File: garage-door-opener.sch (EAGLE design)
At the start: 17 parts, among them IC1 LM2575-3.3T, K1 RR1A, T1 BC547, U1 ESP8266, X2 Connector

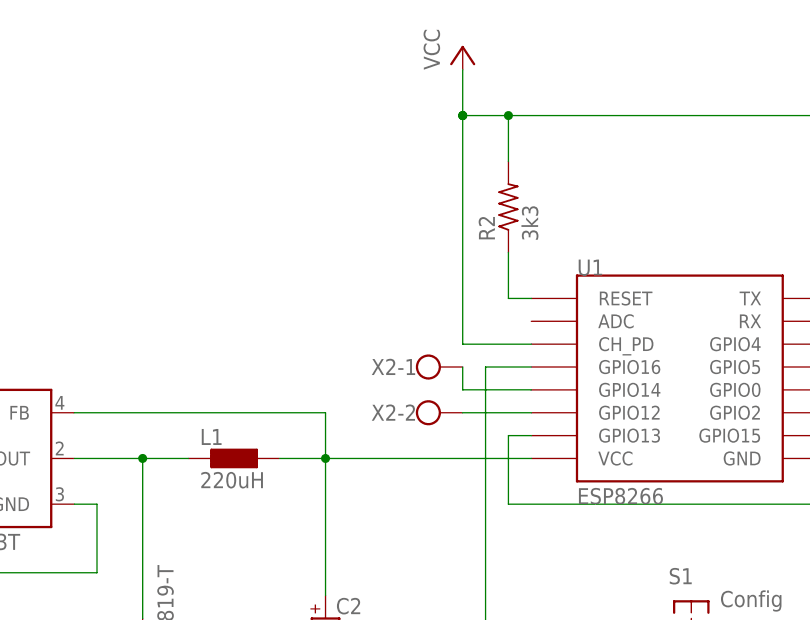
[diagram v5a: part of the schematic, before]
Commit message: removed all the vias. Re-routed some tracks around the developer holes (sort of)
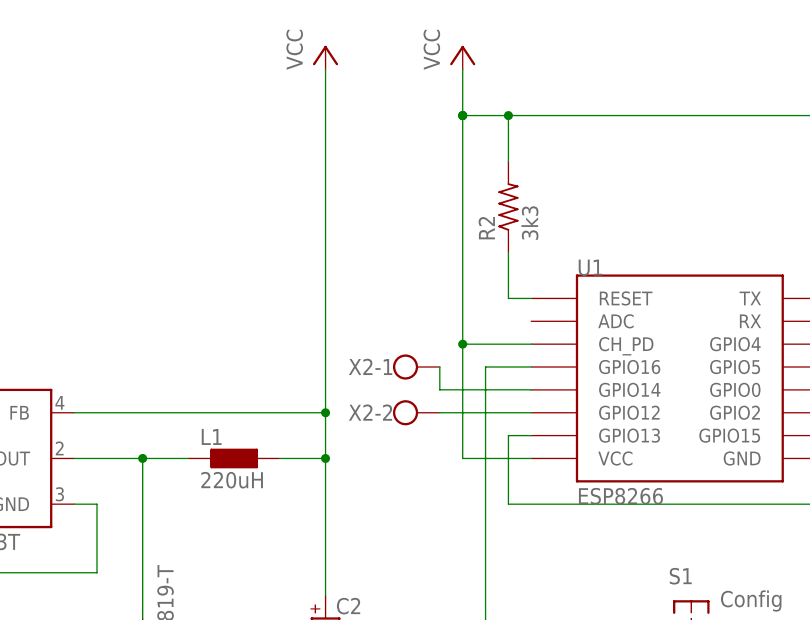
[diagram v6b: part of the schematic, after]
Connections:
- removed net N$4: C2.+, IC1.FB, L1.1, U1.VCC
- net VCC: now also C2.+, IC1.FB, L1.1, U1.VCC
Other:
- moved on the sheet: X2-1, X2-2
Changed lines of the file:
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@@
 <part name="R4" library="resistor" library_urn="urn:adsk.eagle:library:348" deviceset="R-US_" device="0204/7" package3d_urn="urn:adsk.eagle:package:25945/1" value="3k3"/>
 <part name="R5" library="resistor" library_urn="urn:adsk.eagle:library:348" deviceset="R-US_" device="0204/7" package3d_urn="urn:adsk.eagle:package:25945/1" value="3k3"/>
+<part name="P+2" library="supply1" deviceset="VCC" device=""/>
 </parts>
 <sheets>
@@
 <instance part="K1" gate="1" x="162.56" y="60.96"/>
 <instance part="K1" gate="2" x="177.8" y="60.96"/>
-<instance part="X2" gate="-1" x="76.2" y="55.88"/>
-<instance part="X2" gate="-2" x="76.2" y="50.8"/>
+<instance part="X2" gate="-1" x="73.66" y="55.88"/>
+<instance part="X2" gate="-2" x="73.66" y="50.8"/>
 <instance part="X2" gate="-3" x="177.8" y="81.28" rot="R270"/>
 <instance part="X2" gate="-4" x="-7.62" y="50.8" smashed="yes">
@@
 <instance part="R4" gate="G$1" x="83.82" y="15.24" rot="R90"/>
 <instance part="R5" gate="G$1" x="142.24" y="68.58" rot="R90"/>
+<instance part="P+2" gate="VCC" x="66.04" y="91.44"/>
 </instances>
 <busses>
@@
 <wire x1="86.36" y1="78.74" x2="86.36" y2="83.82" width="0.1524" layer="91"/>
 <junction x="86.36" y="83.82"/>
-</segment>
-</net>
-<net name="N$4" class="0">
-<segment>
 <pinref part="U1" gate="G$1" pin="VCC"/>
+<wire x1="88.9" y1="45.72" x2="81.28" y2="45.72" width="0.1524" layer="91"/>
+<wire x1="81.28" y1="45.72" x2="81.28" y2="58.42" width="0.1524" layer="91"/>
+<junction x="81.28" y="58.42"/>
+</segment>
+<segment>
 <pinref part="C2" gate="G$1" pin="+"/>
-<wire x1="66.04" y1="45.72" x2="88.9" y2="45.72" width="0.1524" layer="91"/>
 <wire x1="66.04" y1="30.48" x2="66.04" y2="45.72" width="0.1524" layer="91"/>
 <pinref part="L1" gate="G$1" pin="1"/>
@@
 <wire x1="66.04" y1="45.72" x2="66.04" y2="50.8" width="0.1524" layer="91"/>
 <wire x1="66.04" y1="50.8" x2="38.1" y2="50.8" width="0.1524" layer="91"/>
+<pinref part="P+2" gate="VCC" pin="VCC"/>
+<wire x1="66.04" y1="88.9" x2="66.04" y2="50.8" width="0.1524" layer="91"/>
+<junction x="66.04" y="50.8"/>
 </segment>
 </net>
@@
 <pinref part="X2" gate="-2" pin="KL"/>
 <pinref part="U1" gate="G$1" pin="GPIO12"/>
-<wire x1="81.28" y1="50.8" x2="88.9" y2="50.8" width="0.1524" layer="91"/>
+<wire x1="78.74" y1="50.8" x2="88.9" y2="50.8" width="0.1524" layer="91"/>
 </segment>
 </net>
@@
 <pinref part="X2" gate="-1" pin="KL"/>
 <pinref part="U1" gate="G$1" pin="GPIO14"/>
-<wire x1="81.28" y1="55.88" x2="81.28" y2="53.34" width="0.1524" layer="91"/>
-<wire x1="81.28" y1="53.34" x2="88.9" y2="53.34" width="0.1524" layer="91"/>
-</segment>
-</net>
+<wire x1="78.74" y1="55.88" x2="78.74" y2="53.34" width="0.1524" layer="91"/>
+<wire x1="78.74" y1="53.34" x2="88.9" y2="53.34" width="0.1524" layer="91"/>
+</segment>
+</net>
